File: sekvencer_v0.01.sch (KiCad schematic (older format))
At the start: 98 parts, among them J1 AVR_ISP_01X06, J10 50V_OUT, J11 BIAS, J12 50V_GND, J13 TERMISTOR, J14 50V_GND, J15 50V_GND, J16 50V_GND, J2 PTT, J3 SWR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

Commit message: refactored second version, added bias circuit, fixed layout
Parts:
- added C33, C34: NFM21CC223R1H3D, EMI_Suppression_Filters_Cap_Type:NFM21C_Series, symbol Device:EMI_Filter_C
- added C35: 2u2, Capacitor_SMD:C_0805_2012Metric, symbol Device:C
- added C37: 1u, Capacitor_SMD:C_0805_2012Metric, symbol Device:C
- added D_50V1, D_FAN1, D_PTT1, D_RX1, D_STAT2, D_TX1: LH R974-LP-1, LED_SMD:LED_0805_2012Metric, symbol Device:LED
- added J17: BIAS, Connector_JST:JST_XH_B02B-XH-A_1x02_P2.50mm_Vertical, symbol Connector_Generic:Conn_01x02
- added Q7: BC847, Package_TO_SOT_THT:TO-92, symbol Transistor_BJT:BC847
- added R26, R34: 1k, Resistor_SMD:R_0805_2012Metric, symbol Device:R
- added R27: 12k, Resistor_SMD:R_0805_2012Metric, symbol Device:R
- added R28: 18k, Resistor_SMD:R_0805_2012Metric, symbol Device:R
- added R29, R30, R31: 3k9, Resistor_SMD:R_0805_2012Metric, symbol Device:R
- added R32: 2k2, Resistor_SMD:R_0805_2012Metric, symbol Device:R
- added R33: 10R, Resistor_SMD:R_0805_2012Metric, symbol Device:R
- added R35: 220R, Resistor_SMD:R_0805_2012Metric, symbol Device:R
- added R36: R, Resistor_SMD:R_0805_2012Metric, symbol Device:R
- added RV3, RV4: 10k, Potentiometer_SMD:Potentiometer_Bourns_3214J_Horizontal, symbol Device:POT_TRIM
- added U5: LP2951ACD-3.3R2G, Package_SO:SOIC-8_3.9x4.9mm_P1.27mm, symbol KLALIB_Regulator_Linear:LP2951ACD-3.3R2G
- C21: footprint Capacitor_SMD:C_0805_2012Metric -> Capacitor_THT:CP_Radial_D10.0mm_P5.00mm
- D2: footprint Diode_SMD:D_MELF -> Diode_SMD:D_SOD-123
- D_5V1: renamed from D1; value 5V_LED -> LH R974-LP-1
- D_STAT1: renamed from D7; value STAT_LED -> LH R974-LP-1
- J11: value BIAS -> BIAS_DIRECT
- J5: footprint Connector_JST:JST_EH_B08B-EH-A_1x08_P2.50mm_Vertical -> Connector_JST:JST_EH_B09B-EH-A_1x09_P2.50mm_Vertical; symbol Connector_Generic:Conn_01x08 -> Connector_Generic:Conn_01x09
- R13: value 330R -> 499R
- R14: value 2k -> 10k
- R17: value 12k -> 22k
- R19, R20: value 0R01 -> 0R005
- R2: value 180R -> 1k
- R25: value 1k -> 1k2
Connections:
- net labels added: STATUS_LED1
- net labels removed: STATUS_LED
- wire segments 182 -> 214
- no-connect marks 4 -> 5
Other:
- note added: "0,1V @ 40A\nPztr 4W"
- note added: "For gain 20\nR13 = 499R\nR14 = 10k"
- moved on the sheet: C10, C23, C24, C27, C6, C8, D2, D3, D4, D5, D_STAT1, J1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

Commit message: oficial second version, fixed previous commit
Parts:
- added J18: 50V_GND, MountingHole:MountingHole_3.2mm_M3_Pad_Via, symbol Connector_Specialized:Screw_Terminal_01x01
- J12, J14, J16: footprint MountingHole:MountingHole_4mm_Pad_Via -> MountingHole:MountingHole_4.3mm_M4_Pad_Via
- J15: footprint MountingHole:MountingHole_4mm_Pad_Via -> MountingHole:MountingHole_3.2mm_M3_Pad_Via
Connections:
- net DB5: now also J1.3 (SCK); no longer J1.4 (~RST)
- net DB6: now also J1.4 (~RST); no longer J1.5 (MISO)
- net DB7: now also J1.5 (MISO); no longer J1.6 (MOSI)
- net GND: now also J13.1 (Pin_1), J18.1 (Pin_1); no longer J13.2 (Pin_2)
- net RESET: now also J1.6 (MOSI); no longer J1.3 (SCK)
- net at R17.2, R3.2: now also J13.2 (Pin_2); no longer J13.1 (Pin_1)
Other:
- moved on the sheet: J15, J16
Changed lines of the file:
@@
 L power:GND #PWR012
 U 1 1 5AC9C72F
-P 4600 5950
-F 0 "#PWR012" H 4600 5700 50  0001 C CNN
-F 1 "GND" H 4605 5777 50  0000 C CNN
-F 2 "" H 4600 5950 50  0001 C CNN
-F 3 "" H 4600 5950 50  0001 C CNN
-	1    4600 5950
+P 4600 6350
+F 0 "#PWR012" H 4600 6100 50  0001 C CNN
+F 1 "GND" H 4605 6177 50  0000 C CNN
+F 2 "" H 4600 6350 50  0001 C CNN
+F 3 "" H 4600 6350 50  0001 C CNN
+	1    4600 6350
 	1    0    0    -1
 $EndComp
@@
 $EndComp
 Wire Wire Line
+	10150 6300 9650 6300
+Wire Wire Line
 	10150 6400 9650 6400
 Wire Wire Line
+	10150 6200 9650 6200
+Wire Wire Line
 	10150 6100 9650 6100
-Wire Wire Line
-	10150 6300 9650 6300
-Wire Wire Line
-	10150 6200 9650 6200
+Text Label 9650 6300 0    50   ~ 0
+DB7
 Text Label 9650 6400 0    50   ~ 0
-DB7
+RESET
+Text Label 9650 6200 0    50   ~ 0
+DB6
 Text Label 9650 6100 0    50   ~ 0
-RESET
-Text Label 9650 6300 0    50   ~ 0
-DB6
-Text Label 9650 6200 0    50   ~ 0
 DB5
 $Comp
@@
 F 0 "J12" H 4480 5392 50  0000 L CNN
 F 1 "50V_GND" H 4480 5301 50  0000 L CNN
-F 2 "MountingHole:MountingHole_4mm_Pad_Via" H 4400 5350 50  0001 C CNN
+F 2 "MountingHole:MountingHole_4.3mm_M4_Pad_Via" H 4400 5350 50  0001 C CNN
 F 3 "~" H 4400 5350 50  0001 C CNN
 	1    4400 5350
@@
 L Connector_Generic:Conn_01x02 J13
 U 1 1 5AC4226B
-P 950 7000
-F 0 "J13" H 870 6675 50  0000 C CNN
-F 1 "TERMISTOR" H 870 6766 50  0000 C CNN
-F 2 "Connector_JST:JST_XH_B02B-XH-A_1x02_P2.50mm_Vertical" H 950 7000 50  0001 C CNN
-F 3 "~" H 950 7000 50  0001 C CNN
-	1    950  7000
-	-1   0    0    -1
+P 950 7100
+F 0 "J13" H 870 6775 50  0000 C CNN
+F 1 "TERMISTOR" H 870 6866 50  0000 C CNN
+F 2 "Connector_JST:JST_XH_B02B-XH-A_1x02_P2.50mm_Vertical" H 950 7100 50  0001 C CNN
+F 3 "~" H 950 7100 50  0001 C CNN
+	1    950  7100
+	-1   0    0    1
 $EndComp
 Wire Wire Line
@@
 F 0 "J14" H 4480 5592 50  0000 L CNN
 F 1 "50V_GND" H 4480 5501 50  0000 L CNN
-F 2 "MountingHole:MountingHole_4mm_Pad_Via" H 4400 5550 50  0001 C CNN
+F 2 "MountingHole:MountingHole_4.3mm_M4_Pad_Via" H 4400 5550 50  0001 C CNN
 F 3 "~" H 4400 5550 50  0001 C CNN
 	1    4400 5550
@@
 L Connector_Specialized:Screw_Terminal_01x01 J15
 U 1 1 5ACC1E9F
+P 4400 5950
+F 0 "J15" H 4480 5992 50  0000 L CNN
+F 1 "50V_GND" H 4480 5901 50  0000 L CNN
+F 2 "MountingHole:MountingHole_3.2mm_M3_Pad_Via" H 4400 5950 50  0001 C CNN
+F 3 "~" H 4400 5950 50  0001 C CNN
+	1    4400 5950
+	-1   0    0    1
+$EndComp
+Connection ~ 4600 5750
+$Comp
+L Connector_Specialized:Screw_Terminal_01x01 J16
+U 1 1 5ACC1F79
 P 4400 5750
-F 0 "J15" H 4480 5792 50  0000 L CNN
+F 0 "J16" H 4480 5792 50  0000 L CNN
 F 1 "50V_GND" H 4480 5701 50  0000 L CNN
-F 2 "MountingHole:MountingHole_4mm_Pad_Via" H 4400 5750 50  0001 C CNN
+F 2 "MountingHole:MountingHole_4.3mm_M4_Pad_Via" H 4400 5750 50  0001 C CNN
 F 3 "~" H 4400 5750 50  0001 C CNN
 	1    4400 5750
-	-1   0    0    1
-$EndComp
-Connection ~ 4600 5750
-$Comp
-L Connector_Specialized:Screw_Terminal_01x01 J16
-U 1 1 5ACC1F79
-P 4400 5950
-F 0 "J16" H 4480 5992 50  0000 L CNN
-F 1 "50V_GND" H 4480 5901 50  0000 L CNN
-F 2 "MountingHole:MountingHole_4mm_Pad_Via" H 4400 5950 50  0001 C CNN
-F 3 "~" H 4400 5950 50  0001 C CNN
-	1    4400 5950
 	-1   0    0    1
 $EndComp
@@
 	14300 3950 14300 4100
 Connection ~ 14300 4100
+Wire Wire Line
+	4600 5950 4600 6150
+$Comp
+L Connector_Specialized:Screw_Terminal_01x01 J18
+U 1 1 5ACE25F3
+P 4400 6150
+F 0 "J18" H 4480 6192 50  0000 L CNN
+F 1 "50V_GND" H 4480 6101 50  0000 L CNN
+F 2 "MountingHole:MountingHole_3.2mm_M3_Pad_Via" H 4400 6150 50  0001 C CNN
+F 3 "~" H 4400 6150 50  0001 C CNN
+	1    4400 6150
+	-1   0    0    1
+$EndComp
+Connection ~ 4600 6150
+Wire Wire Line
+	4600 6150 4600 6350
 $EndSCHEMATC

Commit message: third version, sent to fabrication in allpcb
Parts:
- removed Y1: 16MHz, Crystal:Crystal_SMD_2520-4Pin_2.5x2.0mm, symbol Device:Crystal_Small
- added C36, C38, C39: NFM21CC223R1H3D, EMI_Suppression_Filters_Cap_Type:NFM21C_Series, symbol Device:EMI_Filter_C
- added J19: 50V_GND, MountingHole:MountingHole_3.2mm_M3_Pad_Via, symbol Connector_Specialized:Screw_Terminal_01x01
- added L6, L7, L8: BLM31PG500SN1L, Capacitor_SMD:C_1206_3216Metric, symbol Device:Ferrite_Bead
- added TP1: ADC_UCC, TestPoint:TestPoint_Pad_D2.0mm, symbol Connector_Specialized:Test_Point_Probe
- added TP2: +5V, TestPoint:TestPoint_Pad_D2.0mm, symbol Connector_Specialized:Test_Point_Probe
- added TP3: +12V, TestPoint:TestPoint_Pad_D2.0mm, symbol Connector_Specialized:Test_Point_Probe
- added TP4: ADC ICC, TestPoint:TestPoint_Pad_D2.0mm, symbol Connector_Specialized:Test_Point_Probe
- added TP5: GND, TestPoint:TestPoint_Pad_D2.0mm, symbol Connector_Specialized:Test_Point_Probe
- added Y1: 16MHz, KLALIB_Crystal:Crystal_SMD_2520-4Pin_2.5x2.0mm, symbol Device:Crystal_GND24_Small
- C31, C32: value 22p -> 15p
- J12, J14, J16: footprint MountingHole:MountingHole_4.3mm_M4_Pad_Via -> MountingHole:MountingHole_3.2mm_M3_Pad_Via
- R36: value R -> 470R
- renumbered D_STAT2 to D_3V3
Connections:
- net +12V: now also J8.2 (Pin_2), TP3.1; no longer J8.1 (Pin_1)
- net +50V: now also L8.1; no longer R13.2
- net +5V: now also C35.1, U5.8 (IN), TP2.1
- net ADC_ICC: now also TP4.1
- net ADC_UCC: now also TP1.1
- net GND: now also J11.2 (Pin_2), J2.2 (Pin_2), J3.2 (Pin_2), C36.2, C38.2, C39.2, J19.1 (Pin_1), TP5.1, Y1.2, Y1.4; no longer J11.1 (Pin_1), J2.1 (Pin_1), J3.1 (Pin_1)
- net MCU_BIAS: now also J11.1 (Pin_1), U5.3 (SHUTDOWN); no longer C35.1, J11.2 (Pin_2), U5.8 (IN)
- net at C31.1, U1.7 (XTAL1/PB6): now also Y1.3
- net at C32.1, U1.8 (XTAL2/PB7): now also Y1.1
- net at Q4.3 (D), R31.2: now also J8.1 (Pin_1); no longer J8.2 (Pin_2)
- net at R7.2: now also J2.1 (Pin_1); no longer J2.2 (Pin_2)
- net at R23.2: now also J3.1 (Pin_1); no longer J3.2 (Pin_2)
- net at U4.3 (-): now also R13.2; no longer R13.1
- net at Q5.3 (S), R19.1, R20.1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: now also L7.1; no longer U4.4 (+)
- net at RV4.2: now also C36.1; no longer J17.1 (Pin_1)
- new net: C39.1, U4.4 (+)
- new net: C38.1, R13.1
- new net: C38.3, L8.2
- new net: C36.3, L6.2
- new net: J17.1 (Pin_1), L6.1
- new net: C39.3, L7.2
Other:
- moved on the sheet: C1, C11, C12, C19, C2, C22, C23, C24, C25, C29, C3, C30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

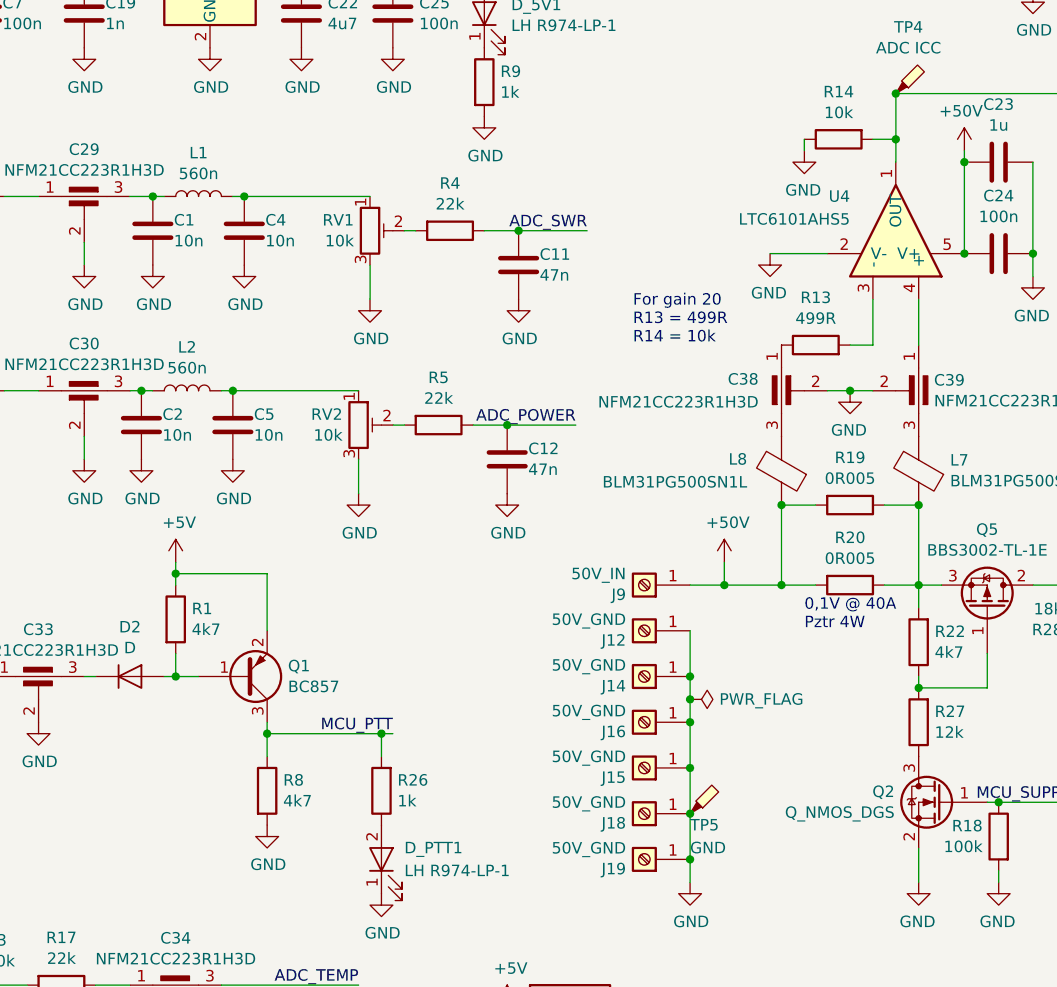
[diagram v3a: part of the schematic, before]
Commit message: in schematic edit value of any components, added some docs
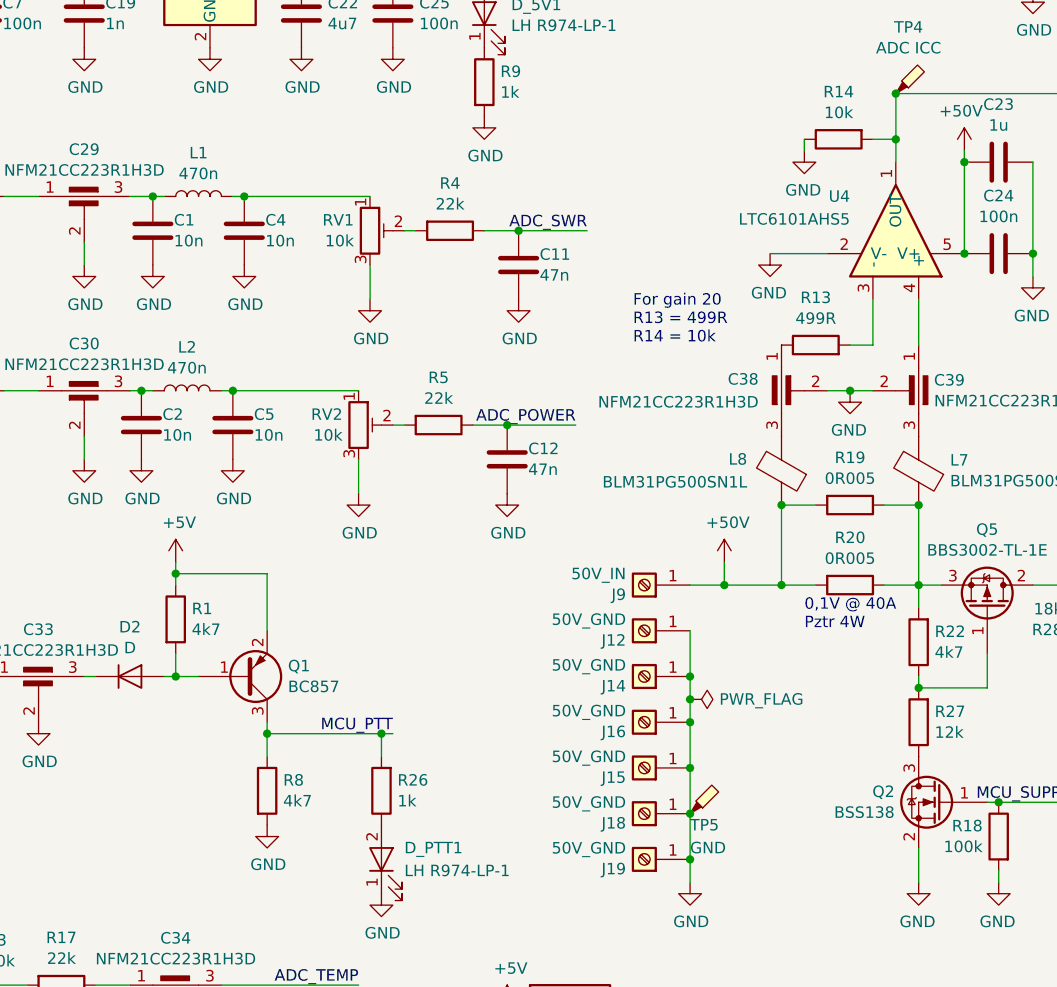
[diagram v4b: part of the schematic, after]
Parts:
- L1, L2: value 560n -> 470n
- Q2: value Q_NMOS_DGS -> BSS138
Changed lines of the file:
@@
 P 1950 3450
 F 0 "L1" V 2140 3450 50  0000 C CNN
-F 1 "560n" V 2049 3450 50  0000 C CNN
+F 1 "470n" V 2049 3450 50  0000 C CNN
 F 2 "Inductor_SMD:L_0805_2012Metric_Pad1.15x1.50mm_HandSolder" H 1950 3450 50  0001 C CNN
 F 3 "~" H 1950 3450 50  0001 C CNN
@@
 P 1900 4300
 F 0 "L2" V 2090 4300 50  0000 C CNN
-F 1 "560n" V 1999 4300 50  0000 C CNN
+F 1 "470n" V 1999 4300 50  0000 C CNN
 F 2 "Inductor_SMD:L_0805_2012Metric_Pad1.15x1.50mm_HandSolder" H 1900 4300 50  0001 C CNN
 F 3 "~" H 1900 4300 50  0001 C CNN
@@
 P 5200 6100
 F 0 "Q2" H 5405 6146 50  0000 L CNN
-F 1 "Q_NMOS_DGS" H 5405 6055 50  0000 L CNN
+F 1 "BSS138" H 5405 6055 50  0000 L CNN
 F 2 "Package_TO_SOT_SMD:SOT-23" H 5400 6200 50  0001 C CNN
 F 3 "https://www.tme.eu/cz/Document/6c7ba86a4db59a0411a4966dbe2bd1aa/BSS123-7-F.pdf" H 5200 6100 50  0001 C CNN

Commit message: added some docs and outputs
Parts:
- D2, D4, D5: value D -> 1N4148
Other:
- note added: "MISO\n"
- note added: "MOSI\n"
- note added: "SCK\n"
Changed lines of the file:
@@
 P 10250 1150
 F 0 "D4" V 10204 1229 50  0000 L CNN
-F 1 "D" V 10295 1229 50  0000 L CNN
+F 1 "1N4148" V 10295 1229 50  0000 L CNN
 F 2 "Diode_SMD:D_MELF" H 10250 1150 50  0001 C CNN
 F 3 "~" H 10250 1150 50  0001 C CNN
@@
 P 10250 2550
 F 0 "D5" V 10204 2629 50  0000 L CNN
-F 1 "D" V 10295 2629 50  0000 L CNN
+F 1 "1N4148" V 10295 2629 50  0000 L CNN
 F 2 "Diode_SMD:D_MELF" H 10250 2550 50  0001 C CNN
 F 3 "~" H 10250 2550 50  0001 C CNN
@@
 P 1650 5550
 F 0 "D2" H 1650 5766 50  0000 C CNN
-F 1 "D" H 1650 5675 50  0000 C CNN
+F 1 "1N4148" H 1650 5675 50  0000 C CNN
 F 2 "Diode_SMD:D_SOD-123" H 1650 5550 50  0001 C CNN
 F 3 "~" H 1650 5550 50  0001 C CNN
@@
 	0    -1   -1   0
 $EndComp
+Text Notes 2575 7200 0    50   ~ 0
+MOSI\n
+Text Notes 2575 7300 0    50   ~ 0
+MISO\n
+Text Notes 2575 7400 0    50   ~ 0
+SCK\n
 $EndSCHEMATC

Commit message: first revision, added resistor and diode in bias circuit
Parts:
- removed R24: 1k, Resistor_SMD:R_0805_2012Metric, symbol Device:R
- added D1: BAS7002VH6327XTSA1, Diode_SMD:D_SOD-523, symbol Device:D_Schottky
- added L10, L9: BLM31PG500SN1L, Capacitor_SMD:C_1206_3216Metric, symbol Device:Ferrite_Bead
- J10, J12, J14, J15, J16, J18, J19, J9: symbol Connector_Specialized:Screw_Terminal_01x01 -> Connector_Generic:Conn_01x01
- R23: value 1k -> 100k; footprint Resistor_SMD:R_0805_2012Metric -> Resistor_SMD:R_0402_1005Metric
- RV1, RV2, RV3, RV4: symbol Device:POT_TRIM -> Device:R_POT
- TP1, TP2, TP3, TP4, TP5: symbol Connector_Specialized:Test_Point_Probe -> Connector_Generic:Conn_01x01
- Y1: value 16MHz -> LFXTAL071268CUTT 16MHz
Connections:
- wire segments 223 -> 222
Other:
- moved on the sheet: C31, C32, C35, C36, C37, D_3V3, D_FAN1, D_STAT1, J11, J17, J5, J8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

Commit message: hiearchic
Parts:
- removed C13: 1n, Capacitor_SMD:C_0805_2012Metric, symbol Device:C
- removed C14: 100p, Capacitor_SMD:C_0805_2012Metric, symbol Device:C
- removed C20, C27: 100n, Capacitor_SMD:C_0805_2012Metric, symbol Device:C
- removed C21: 100u, Capacitor_THT:CP_Radial_D10.0mm_P5.00mm, symbol Device:CP
- removed C26: 470u, Capacitor_THT:CP_Radial_D10.0mm_P5.00mm, symbol Device:CP
- removed C28: NFM21CC223R1H3D, EMI_Suppression_Filters_Cap_Type:NFM21C_Series, symbol Device:EMI_Filter_C
- removed C9: 10n, Capacitor_SMD:C_0805_2012Metric, symbol Device:C
- removed D6: STPS3L60U, Diode_SMD:D_SMB, symbol Device:D_Schottky
- removed L4: DE1209-230u, Inductor_SMD:L_12x12mm_H8mm, symbol Device:L
- removed L5: BLM31PG500SN1L, Capacitor_SMD:C_1206_3216Metric, symbol Device:Ferrite_Bead
- removed R15: 270k, Resistor_SMD:R_0805_2012Metric, symbol Device:R
- removed R16: 10k, Resistor_SMD:R_0805_2012Metric, symbol Device:R
- removed TP1: ADC_UCC, TestPoint:TestPoint_Pad_D2.0mm, symbol Connector_Generic:Conn_01x01
- removed TP3: +12V, TestPoint:TestPoint_Pad_D2.0mm, symbol Connector_Generic:Conn_01x01
- removed U3: LM2576HVS-12, Package_TO_SOT_SMD:TO-263-5_TabPin3, symbol Regulator_Switching:LM2576HVS-12
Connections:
- wire segments 222 -> 195

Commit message: add partial schematics images, complete schematic good version for publi
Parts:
- removed D_3V3, D_5V1, D_FAN1, D_PTT1, D_RX1, D_TX1: LH R974-LP-1, LED_SMD:LED_0805_2012Metric, symbol Device:LED
- added C13: 1n, Capacitor_SMD:C_0805_2012Metric, symbol Device:C
- added C14: 100p, Capacitor_SMD:C_0805_2012Metric, symbol Device:C
- added C20, C27: 100n, Capacitor_SMD:C_0805_2012Metric, symbol Device:C
- added C21: 100u, Capacitor_THT:CP_Radial_D10.0mm_P5.00mm, symbol Device:CP
- added C26: 470u, Capacitor_THT:CP_Radial_D10.0mm_P5.00mm, symbol Device:CP
- added C28: NFM21CC223R1H3D, EMI_Suppression_Filters_Cap_Type:NFM21C_Series, symbol Device:EMI_Filter_C
- added C9: 10n, Capacitor_SMD:C_0805_2012Metric, symbol Device:C
- added D10: FAN, LED_SMD:LED_0805_2012Metric, symbol Device:LED
- added D11: +5V, LED_SMD:LED_0805_2012Metric, symbol Device:LED
- added D12: PTT, LED_SMD:LED_0805_2012Metric, symbol Device:LED
- added D13: 3.3V, LED_SMD:LED_0805_2012Metric, symbol Device:LED
- added D6: STPS3L60U, Diode_SMD:D_SMB, symbol Device:D_Schottky
- added D8: REL1, LED_SMD:LED_0805_2012Metric, symbol Device:LED
- added D9: REL2, LED_SMD:LED_0805_2012Metric, symbol Device:LED
- added L4: DE1209-230u, Inductor_SMD:L_12x12mm_H8mm, symbol Device:L
- added L5: BLM31PG500SN1L, Capacitor_SMD:C_1206_3216Metric, symbol Device:Ferrite_Bead
- added R15: 270k, Resistor_SMD:R_0805_2012Metric, symbol Device:R
- added R16: 10k, Resistor_SMD:R_0805_2012Metric, symbol Device:R
- added TP1: ADC_UCC, TestPoint:TestPoint_Pad_D2.0mm, symbol Connector_Generic:Conn_01x01
- added TP3: +12V, TestPoint:TestPoint_Pad_D2.0mm, symbol Connector_Generic:Conn_01x01
- added U3: LM2576HVS-12, Package_TO_SOT_SMD:TO-263-5_TabPin3, symbol Regulator_Switching:LM2576HVS-12
- D7: renamed from D_STAT1; value LH R974-LP-1 -> STAT1; Součástka (none) -> LH R974-LP-1
- J4: value POWER -> PWR
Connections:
- net labels added: ADC_PWR, XTAL1, XTAL2
- net labels removed: 2,5Vref, ADC_POWER
- wire segments 195 -> 231
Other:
- moved on the sheet: C1, C10, C11, C12, C15, C16, C17, C18, C19, C2, C22, C23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
